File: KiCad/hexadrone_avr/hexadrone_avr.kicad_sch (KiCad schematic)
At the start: 10 parts, among them P1 LCD1602_I2C, P2 Buzzer, P3 MPU-9250/6500, P4 HC-SR04, P5 VL53L0/1XV2

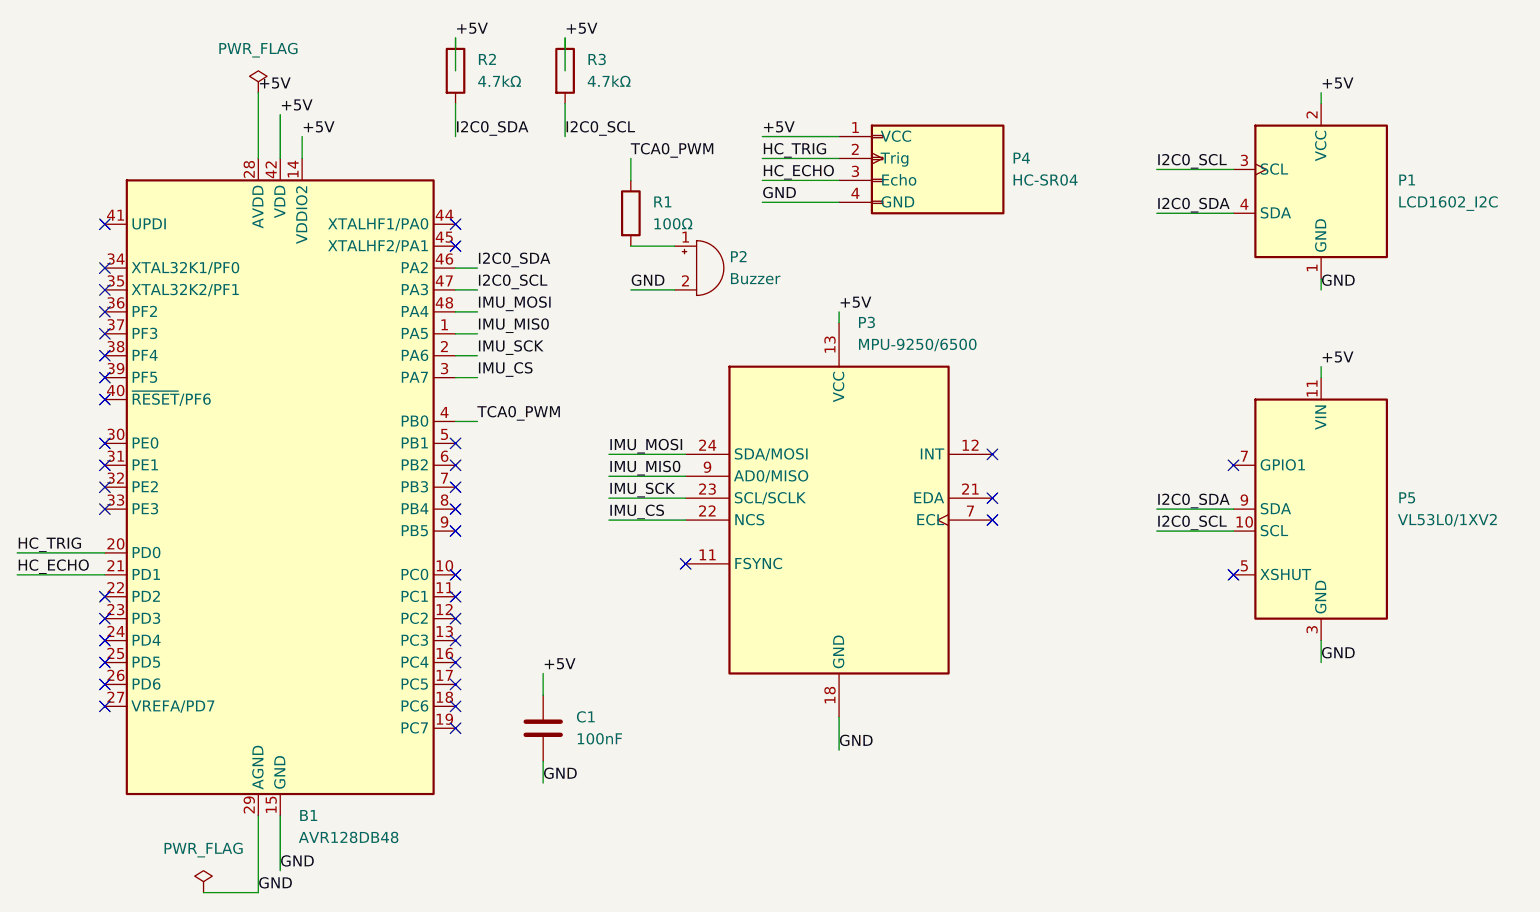
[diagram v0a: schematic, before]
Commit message: Working version, >90 degree tilt bug persists (not critical for a ground stable platform)
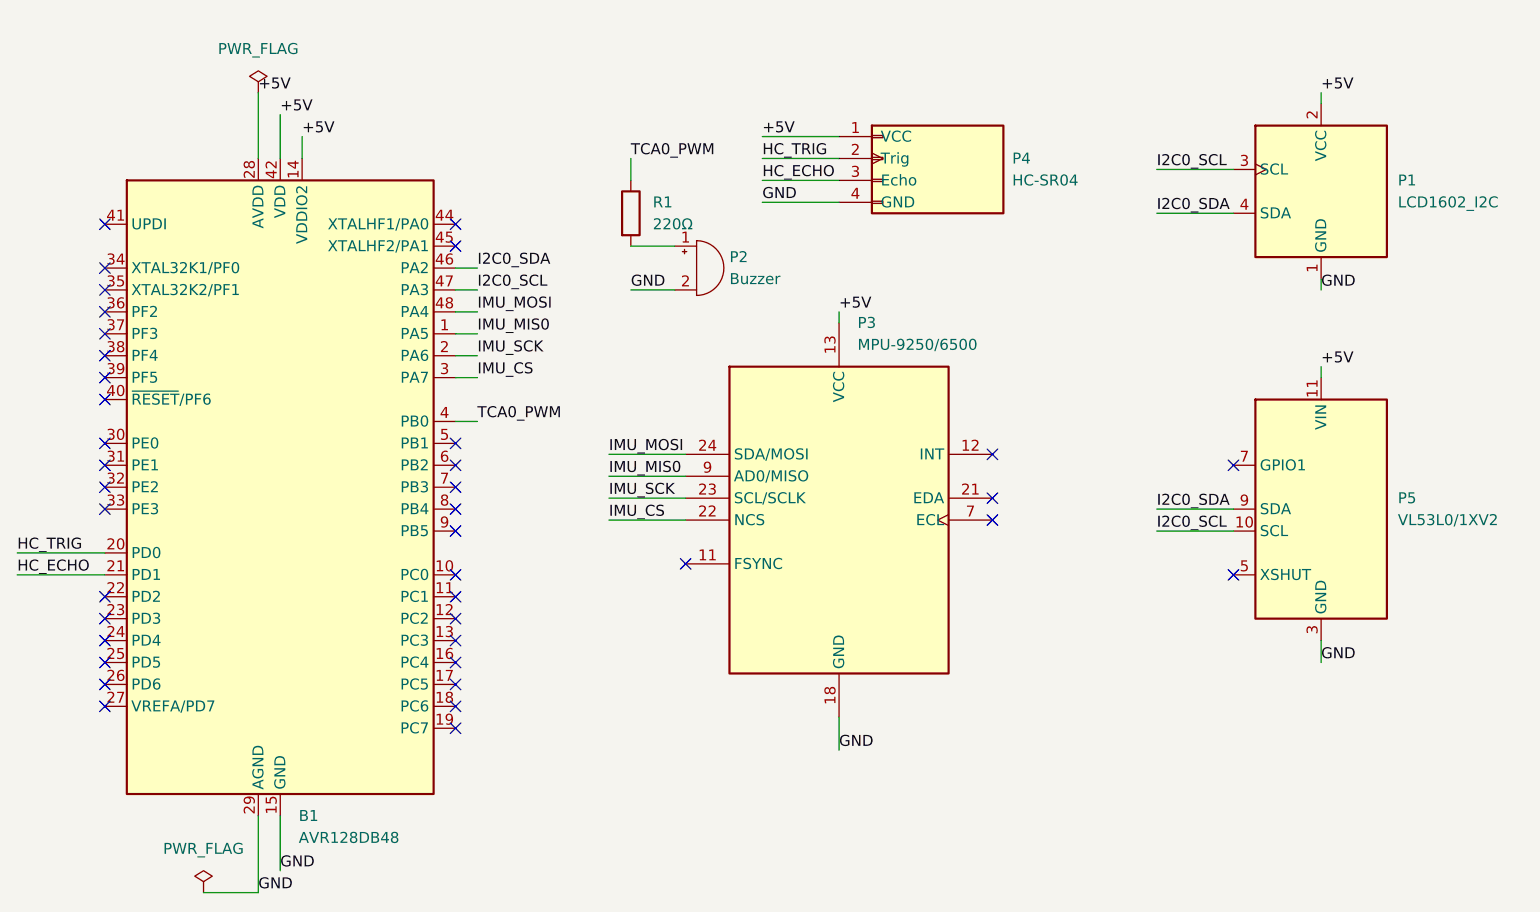
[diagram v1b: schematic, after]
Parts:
- removed C1: 100nF, symbol Device:C
- removed R2, R3: 4.7kΩ, symbol Device:R
- R1: value 100Ω -> 220Ω
